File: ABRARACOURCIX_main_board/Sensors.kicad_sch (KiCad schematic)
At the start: 1 part, among them U2 ICM-42688-P

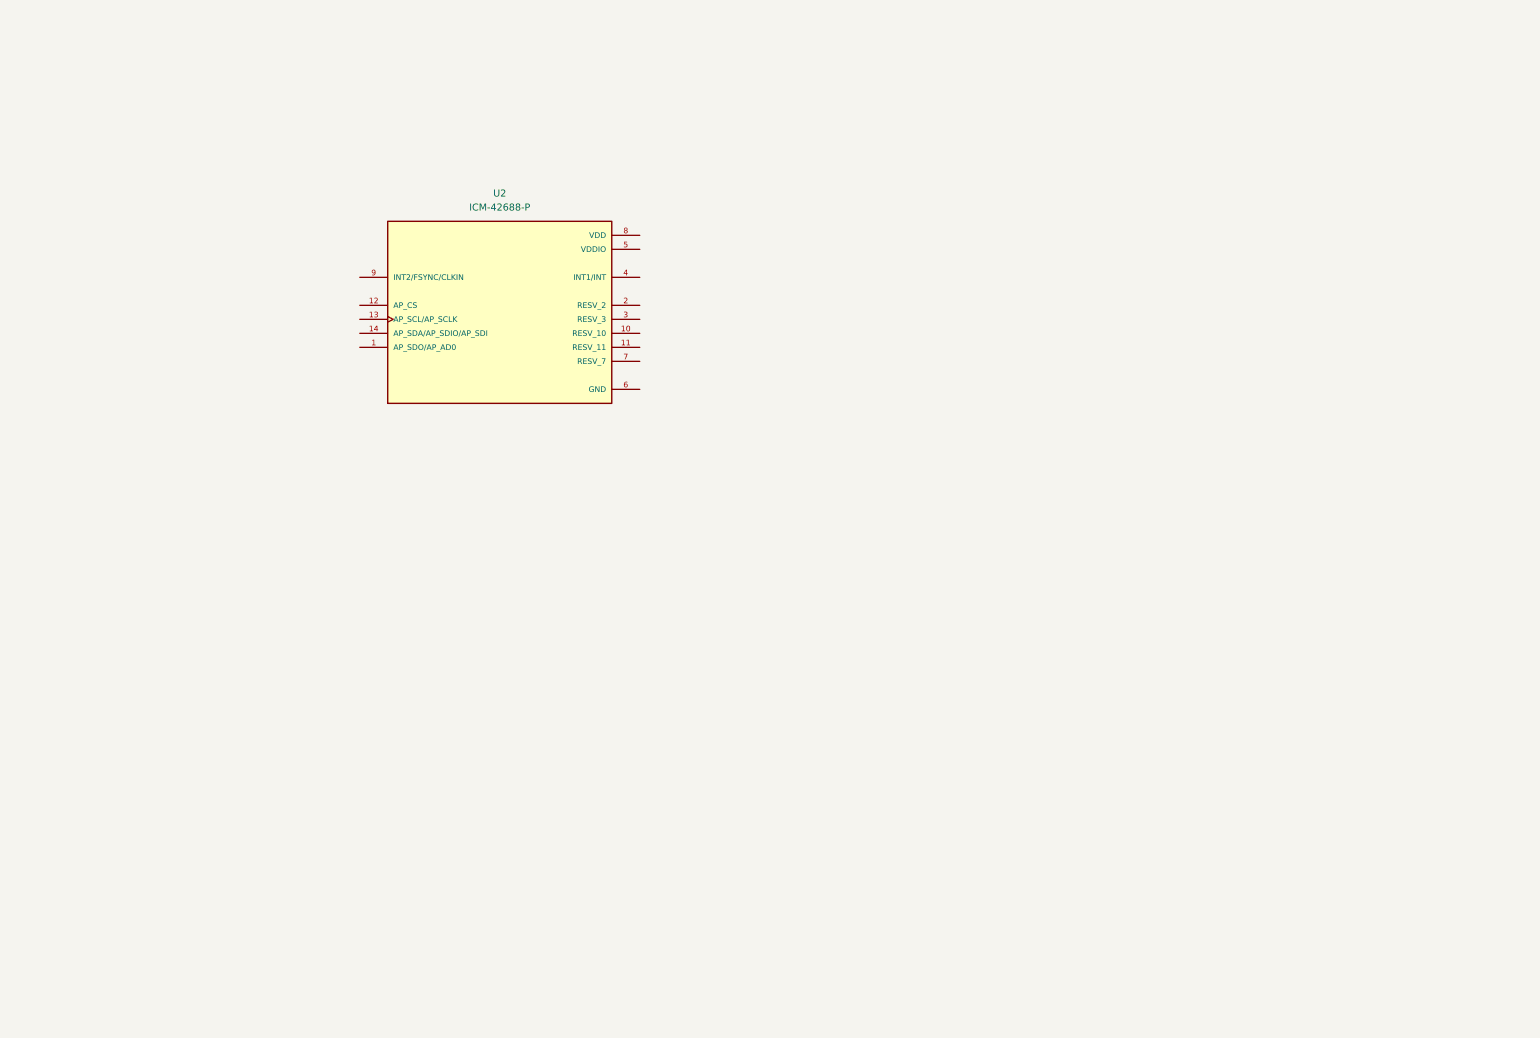
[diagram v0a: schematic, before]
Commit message: Avancement
Decoupling caps
Changement de stm32
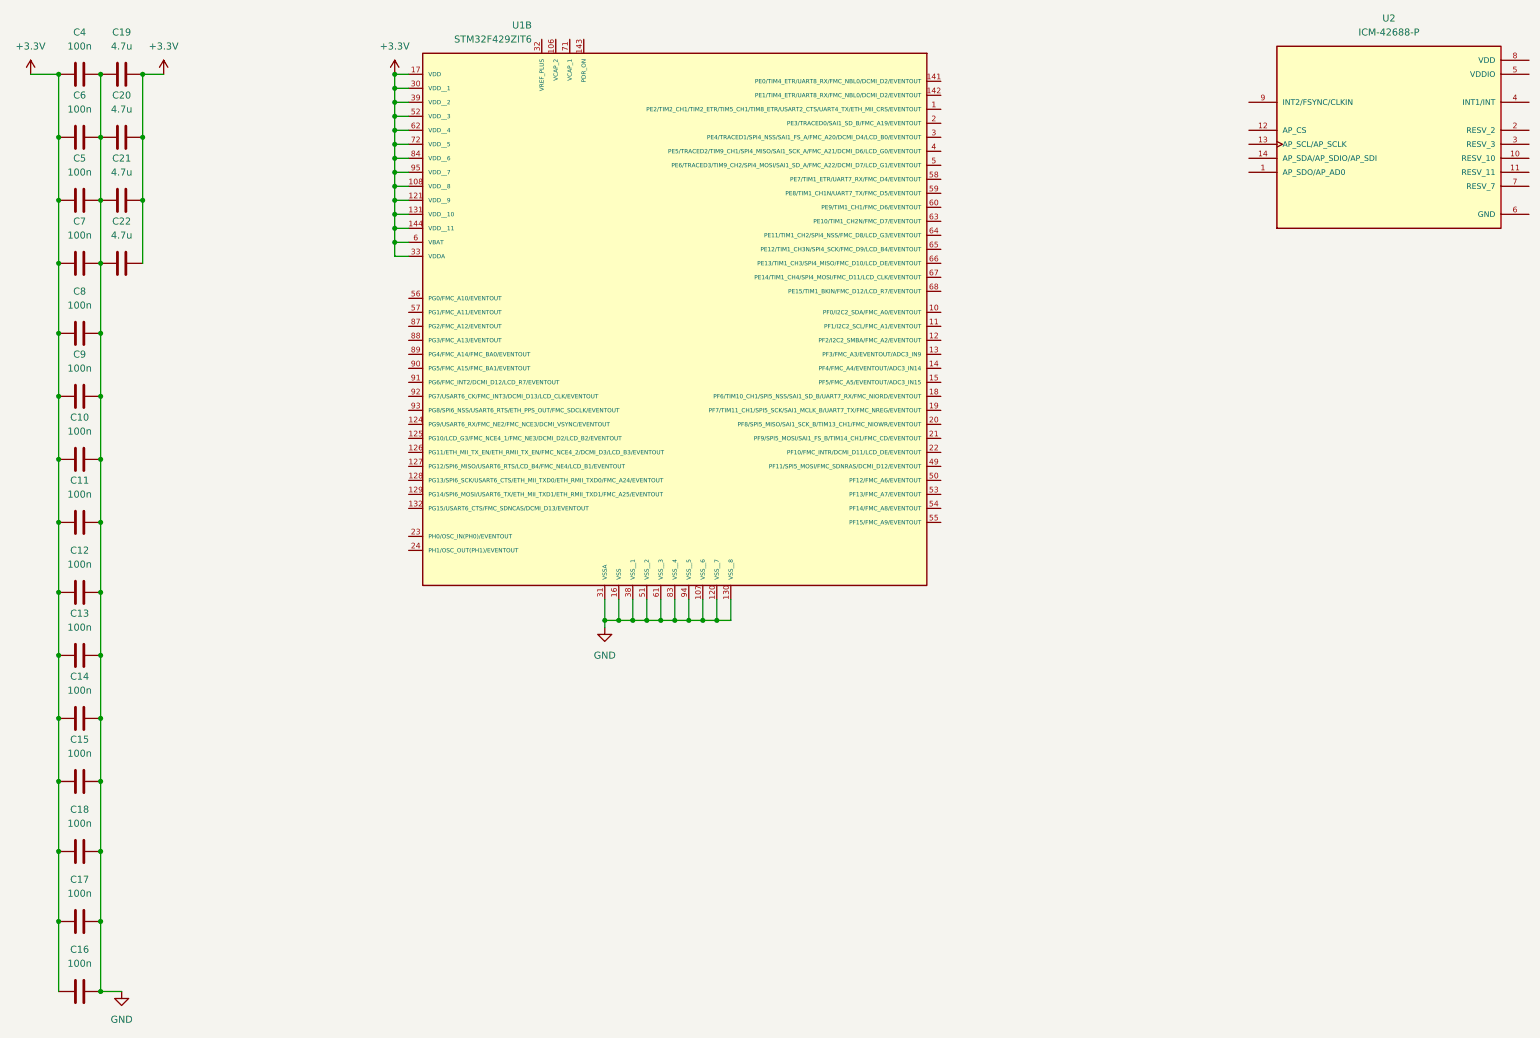
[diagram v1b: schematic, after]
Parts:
- added C10, C11, C12, C13, C14, C15, C16, C17, C18, C4, C5, C6, C7, C8, C9: 100n, symbol Device:C
- added C19, C20, C21, C22: 4.7u, symbol Device:C
- added U1: STM32F429ZIT6, STM32F429ZIT6:QFP50P2200X2200X160-144N, symbol GAUL_ABRARACOURCIX:STM32F429ZIT6
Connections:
- new net +3.3V: C10.1, C11.1, C12.1, C13.1, C14.1, C15.1, C16.1, C17.1, C18.1, C19.2, C20.2, C21.2, C22.2, C4.1, C5.1, C6.1, C7.1, C8.1, C9.1, U1.108 (VDD__8), U1.121 (VDD__9), U1.131 (VDD__10), U1.144 (VDD__11), U1.17 (VDD), U1.30 (VDD__1), U1.33 (VDDA), U1.39 (VDD__2), U1.52 (VDD__3), U1.6 (VBAT), U1.62 (VDD__4), U1.72 (VDD__5), U1.84 (VDD__6), U1.95 (VDD__7)
- new net GND: C10.2, C11.2, C12.2, C13.2, C14.2, C15.2, C16.2, C17.2, C18.2, C19.1, C20.1, C21.1, C22.1, C4.2, C5.2, C6.2, C7.2, C8.2, C9.2, U1.107 (VSS__6), U1.120 (VSS__7), U1.130 (VSS__8), U1.16 (VSS), U1.31 (VSSA), U1.38 (VSS__1), U1.51 (VSS__2), U1.61 (VSS__3), U1.83 (VSS__4), U1.94 (VSS__5)
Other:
- moved on the sheet: U2

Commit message: Commit de kicad
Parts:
- added U5: BNO055, BNO055:LGA28R50P4X10_380X520X100, symbol GAUL_ABRARACOURCIX:BNO055
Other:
- moved on the sheet: U1B, U2
